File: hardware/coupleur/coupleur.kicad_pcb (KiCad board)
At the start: 4 copper layers, 40.1 x 26.1 mm, 3 parts, among them J1 RJ45, J2 RJ45, J3 RJ45

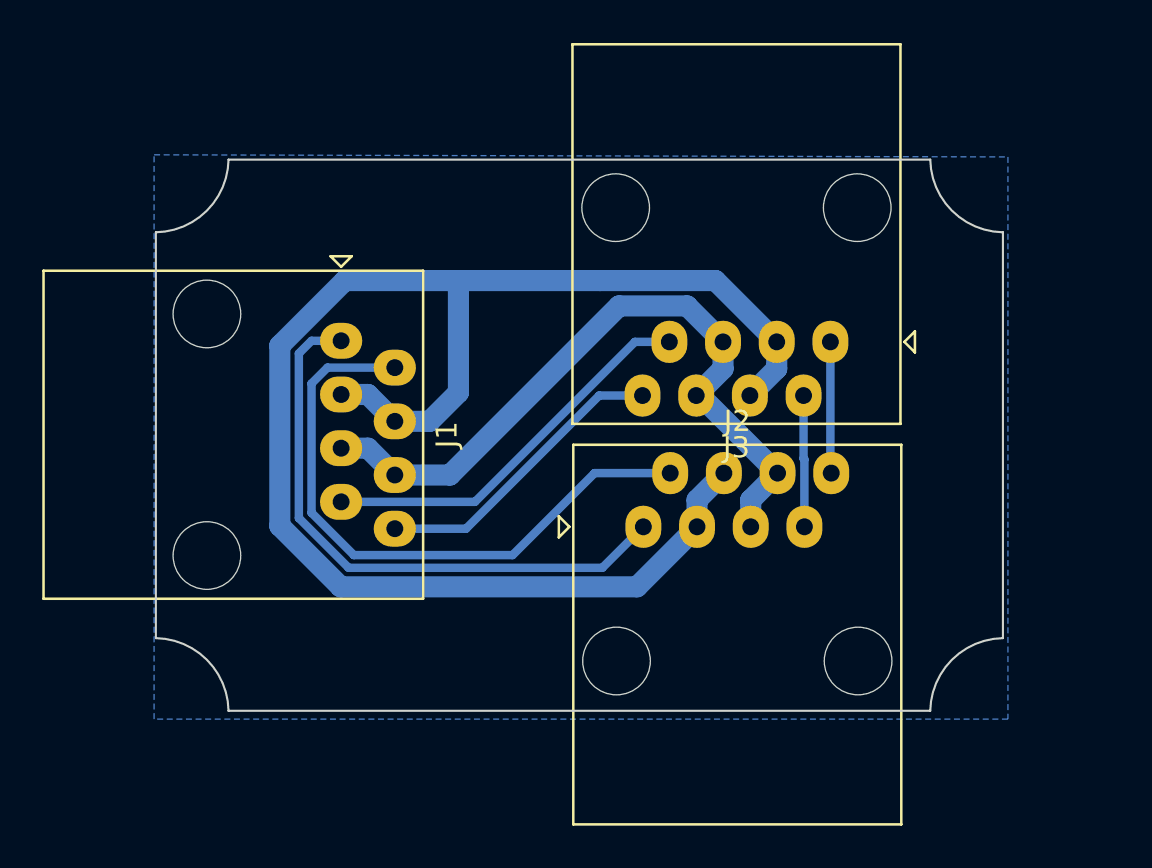
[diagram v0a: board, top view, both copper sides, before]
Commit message: Add 5mm margin around PCBs
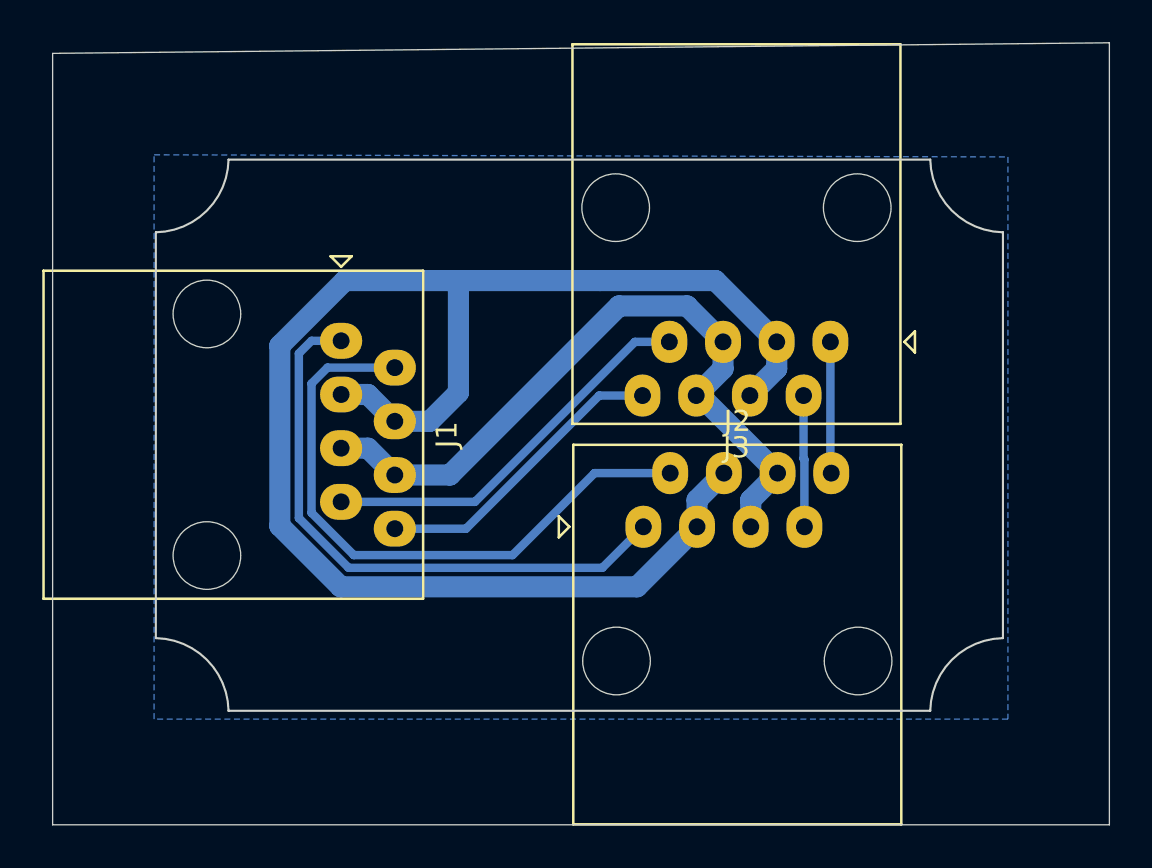
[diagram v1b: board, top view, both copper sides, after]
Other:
- board size 40.1 x 26.1 mm -> 50 x 37 mm

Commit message: Fix edges; only 2 layers
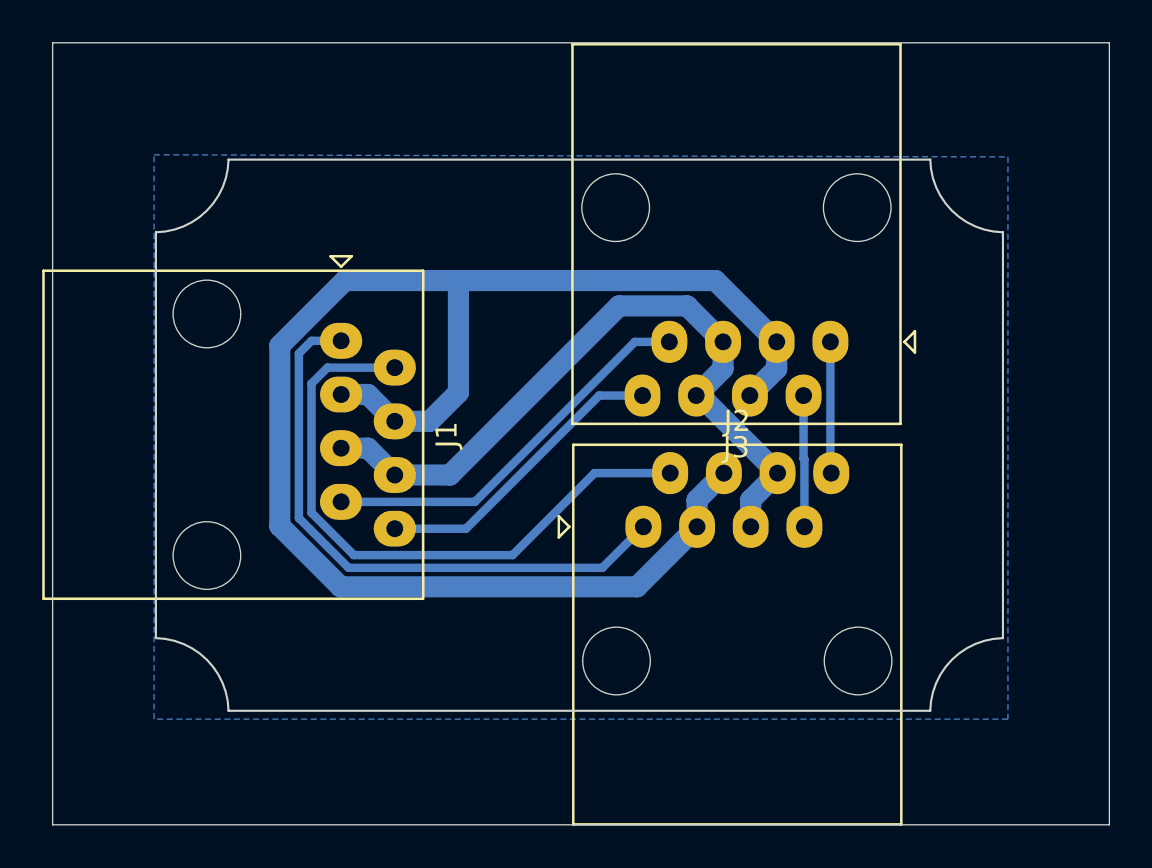
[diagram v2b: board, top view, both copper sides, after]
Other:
- outline, holes or cut-outs redrawn
- copper layers 4 -> 2
